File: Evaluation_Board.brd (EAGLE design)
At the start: 60.9 x 39.4 mm, 41 parts, among them IC1 MEGA32-A, IC2 FT232RL, IC3 317EMP, J1 DCJ0202

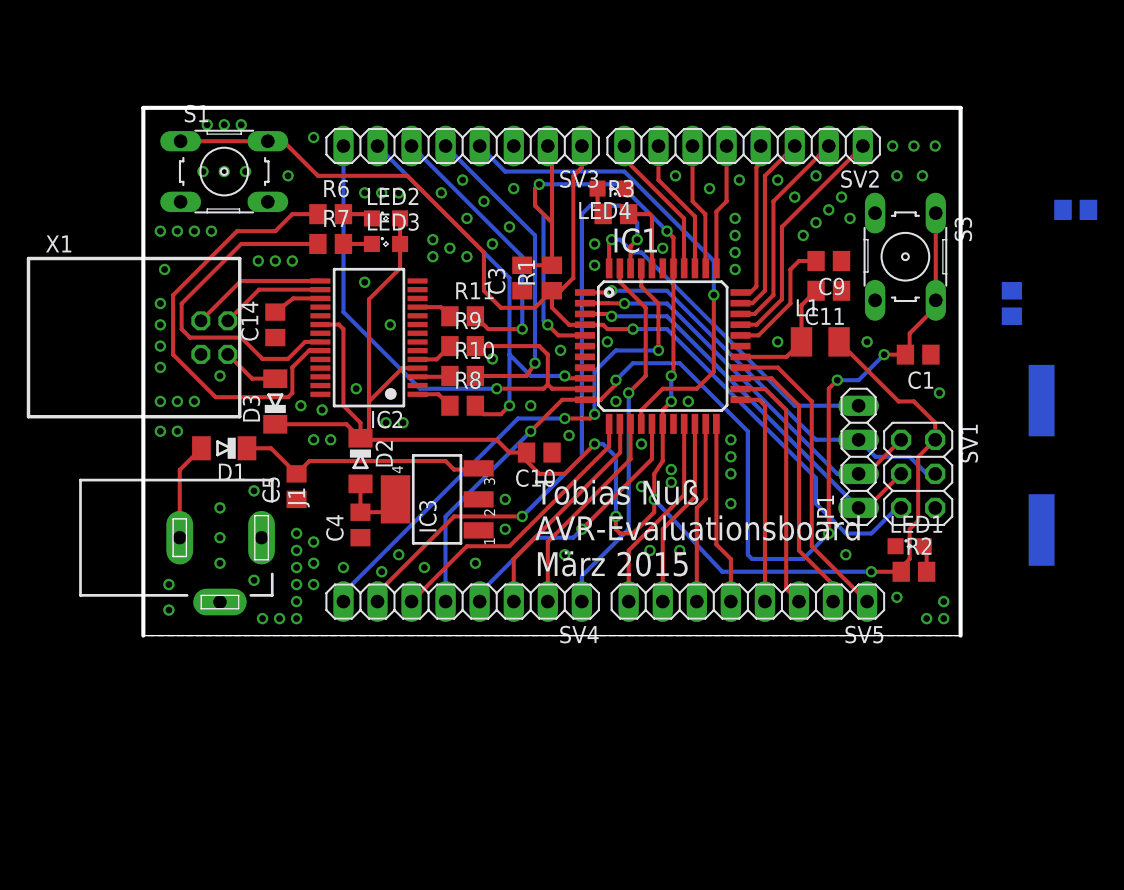
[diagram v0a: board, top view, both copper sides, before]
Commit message: Changed dimension layer to 0 mil -> standard for board outline. Smashed all components to move them and get a better silk screen.
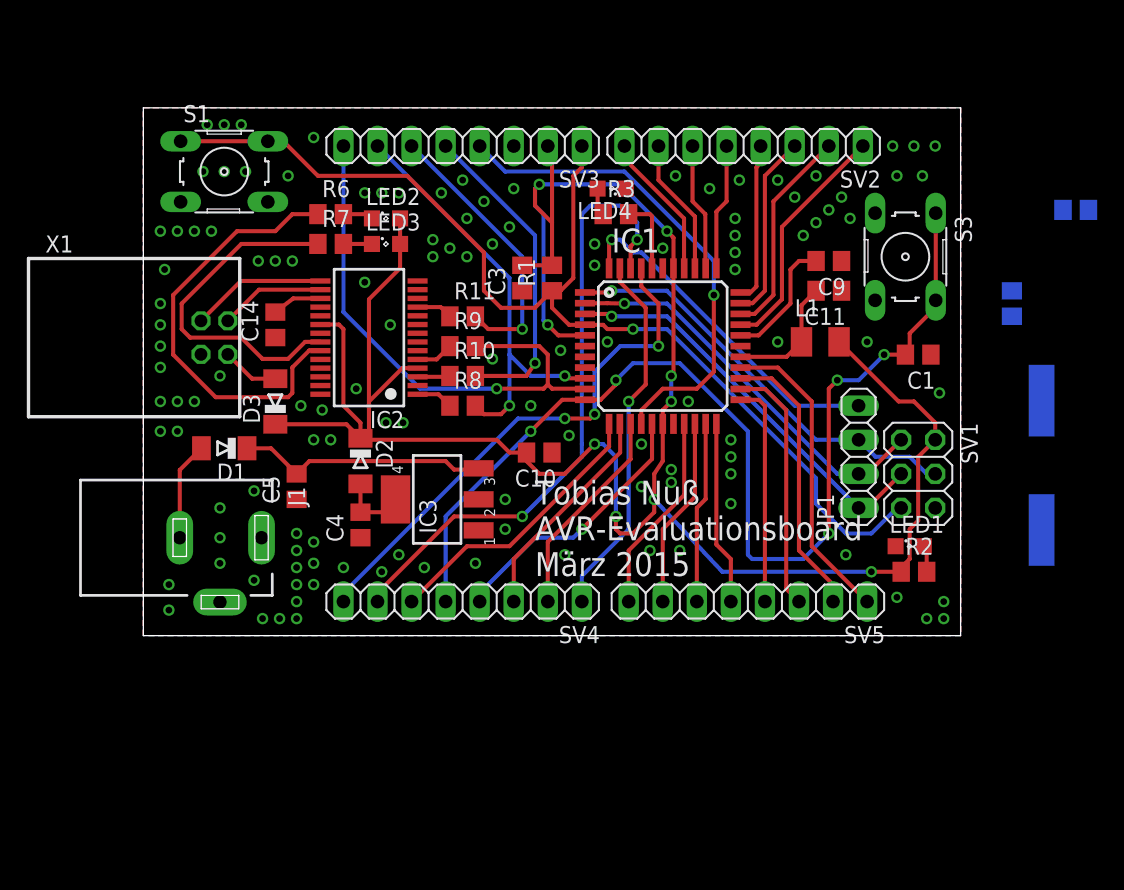
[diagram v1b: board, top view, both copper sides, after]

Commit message: Added crystal to layout and changed the values for both load caps.
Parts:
- C2, C6: value 100n -> 12p
- Q1: value (none) -> 16 MHz
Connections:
- new net N$17: C2.2, IC1.7, Q1.2
- new net N$25: C6.2, IC1.8, Q1.1
- net GND: now also C2.1, C6.1
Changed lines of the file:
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@@
 <attribute name="VALUE" x="12.2555" y="15.8115" size="1.27" layer="27" rot="R90"/>
 </element>
-<element name="C2" library="rcl" package="C0805" value="100n" x="64.77" y="24.765" smashed="yes" rot="MR270">
+<element name="C2" library="rcl" package="C0805" value="12p" x="64.77" y="24.765" smashed="yes" rot="MR270">
 <attribute name="NAME" x="63.5" y="26.035" size="1.27" layer="26" rot="MR270"/>
 <attribute name="VALUE" x="67.31" y="26.035" size="1.27" layer="28" rot="MR270"/>
 </element>
-<element name="C6" library="rcl" package="C0805" value="100n" x="69.5325" y="31.75" smashed="yes" rot="MR180">
+<element name="C6" library="rcl" package="C0805" value="12p" x="69.5325" y="31.75" smashed="yes" rot="MR180">
 <attribute name="NAME" x="68.2625" y="30.48" size="1.27" layer="26" rot="MR180"/>
 <attribute name="VALUE" x="68.2625" y="34.29" size="1.27" layer="28" rot="MR180"/>
 </element>
-<element name="Q1" library="crystal" package="HC49UP" value="" x="66.9925" y="12.7" smashed="yes" rot="MR90">
+<element name="Q1" library="crystal" package="HC49UP" value="16 MHz" x="66.9925" y="12.7" smashed="yes" rot="MR90">
 <attribute name="OC_NEWARK" value="unknown" x="66.9925" y="12.7" size="1.778" layer="28" rot="MR90" display="off"/>
 <attribute name="MPN" value="" x="66.9925" y="12.7" size="1.778" layer="28" rot="MR90" display="off"/>
@@
 <via x="37.1475" y="11.1125" extent="1-16" drill="0.5"/>
 <via x="38.735" y="28.8925" extent="1-16" drill="0.5"/>
+<contactref element="C2" pad="1"/>
+<contactref element="C6" pad="1"/>
+<wire x1="64.77" y1="25.715" x2="68.5825" y2="31.75" width="0" layer="19" extent="16-16"/>
+<wire x1="58.735" y1="20.955" x2="64.77" y2="25.715" width="0" layer="19" extent="1-16"/>
 </signal>
 <signal name="+5V">
@@
 <wire x1="17.8535" y1="9.205" x2="18.8085" y2="10.16" width="0.3048" layer="1"/>
 </signal>
+<signal name="N$17">
+<contactref element="Q1" pad="2"/>
+<contactref element="C2" pad="2"/>
+<contactref element="IC1" pad="7"/>
+<wire x1="66.9925" y1="17.526" x2="64.77" y2="23.815" width="0" layer="19" extent="16-16"/>
+<wire x1="32.935" y1="20.79" x2="64.77" y2="23.815" width="0" layer="19" extent="1-16"/>
+</signal>
+<signal name="N$25">
+<contactref element="Q1" pad="1"/>
+<contactref element="C6" pad="2"/>
+<contactref element="IC1" pad="8"/>
+<wire x1="66.9925" y1="7.874" x2="70.4825" y2="31.75" width="0" layer="19" extent="16-16"/>
+<wire x1="32.935" y1="19.99" x2="66.9925" y2="7.874" width="0" layer="19" extent="1-16"/>
+</signal>
 </signals>

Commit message: Begin of revolution! ;-)
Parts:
- removed R10, R11, R8, R9: 1k, rcl:R0805
- added C7: 100n, rcl:C0805
- moved Q1 43.4 mm to (25.4, 25.2), flipped to the top
- moved C6 40.3 mm to (30.8, 20.8), flipped to the top, turned to 270 degrees
- moved C2 35.4 mm to (29.4, 24.3), flipped to the top
- moved C3 17.2 mm to (33.2, 43.2)
- moved R1 17.2 mm to (35.4, 43.2)
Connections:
- removed net N$21: IC2.1, R8.1
- removed net N$22: IC2.5, R9.1
- removed net N$23: IC2.3, R10.1
- removed net N$24: IC2.11, R11.1
- net +5V: now also C7.2
- net CTS: now also IC2.11; no longer R11.2
- net GND: now also C7.1
- net RTS: now also IC2.3; no longer R10.2
- net RX_USB: now also IC2.1; no longer R8.2
- net TX_USB: now also IC2.5; no longer R9.2
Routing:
- net +5V: track 174.9 -> 129.4 mm, vias 9 -> 7
- net RESET: track 83.3 -> 38.4 mm
- net TX_USB: track 40.9 -> 0.00 mm, vias 1 -> 0
- net RX_USB: track 32.9 -> 0.00 mm, vias 2 -> 0
- net RTS: track 23.9 -> 0.00 mm, vias 1 -> 0
- net CTS: track 21.0 -> 0.00 mm, vias 1 -> 0
- net N$22: track 2.82 -> 0.00 mm
- net N$21: track 2.76 -> 0.00 mm
- net N$24: track 2.69 -> 0.00 mm
- net N$23: track 2.44 -> 0.00 mm
- net PD2_INT0: track 81.1 -> 82.0 mm

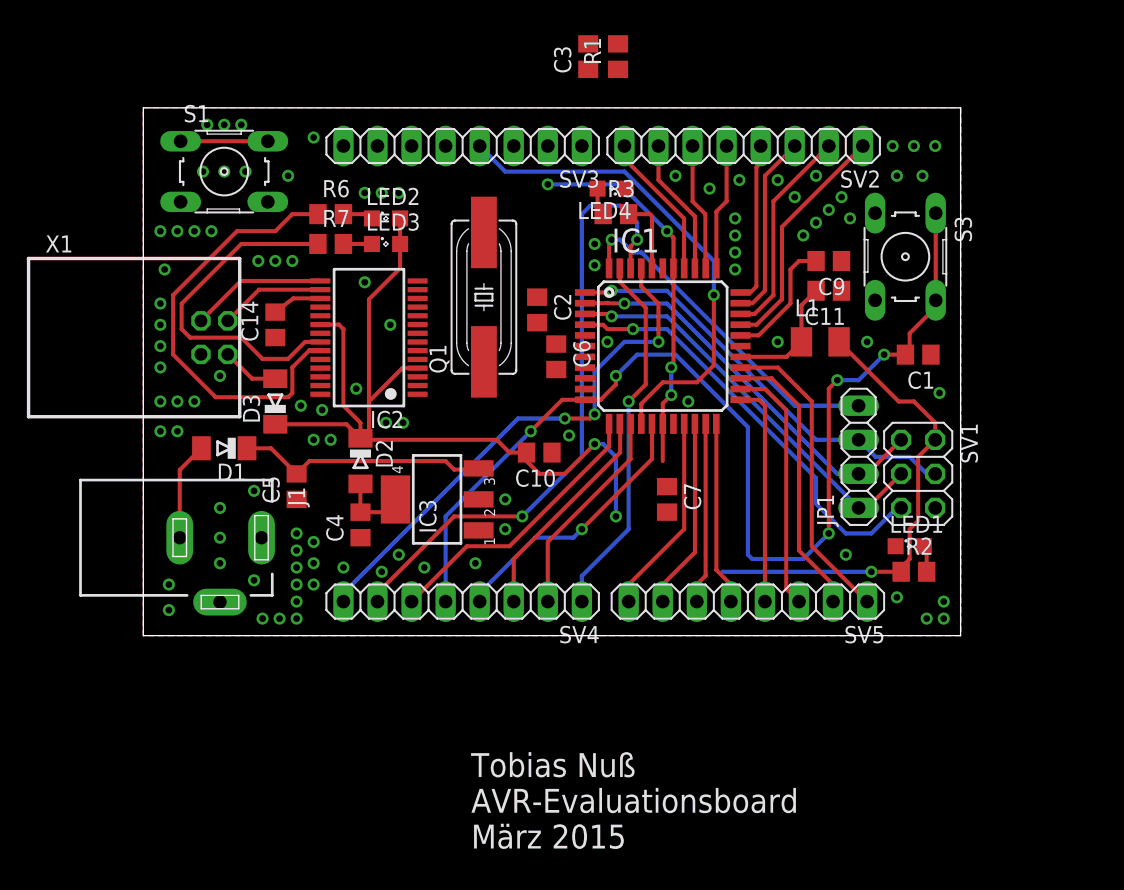
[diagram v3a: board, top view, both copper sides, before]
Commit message: No airwires left, implemented crystal layout and removed the resistors on serial line. Removed diode D2 from voltage regulator and placed as anti parallel diode.
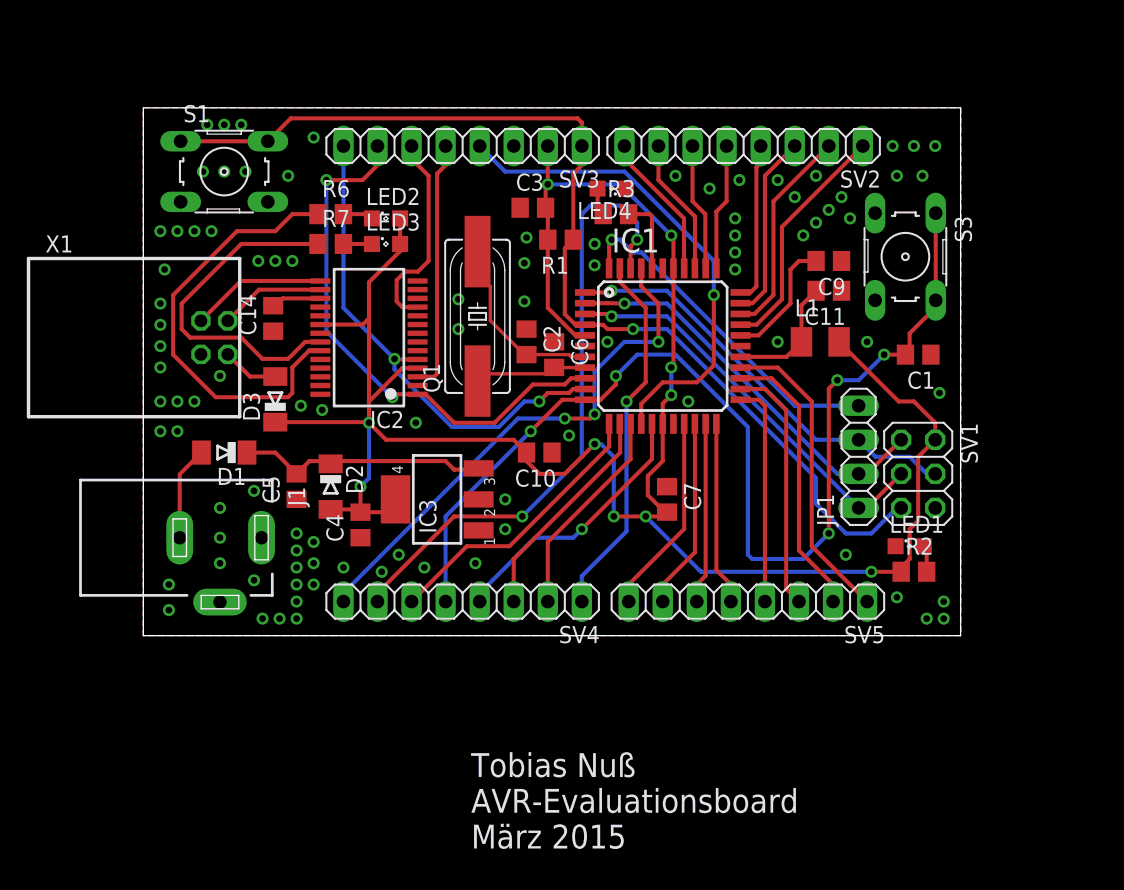
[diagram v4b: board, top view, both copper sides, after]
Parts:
- moved R1 14.3 mm to (31.1, 29.5), turned to 180 degrees
- moved C3 12.0 mm to (29.1, 31.9), turned to 0 degrees
- moved D2 2.93 mm to (14.0, 11.1)
- moved C2 2.51 mm to (28.6, 21.9)
- moved Q1 1.51 mm to (24.9, 23.8)
- moved C14 0.50 mm to (9.68, 23.7)
- moved D1 0.32 mm to (6.03, 13.7)
- moved C6 0.22 mm to (30.6, 21.0)
- moved D3 0.16 mm to (9.84, 17.6)
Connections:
- removed net N$2: C4.2, D2.A, IC3.4
- net +5V: now also C4.2, D2.A, IC3.4; no longer D2.C
- net NETZ: now also D2.C
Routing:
- net RESET: track 38.4 -> 79.3 mm
- net RX_USB: track 0.00 -> 40.6 mm, vias 0 -> 2
- net TX_USB: track 0.00 -> 37.4 mm, vias 0 -> 2
- net +5V: track 129.4 -> 165.6 mm, vias 7 -> 10
- net RTS: track 0.00 -> 18.8 mm
- net CTS: track 0.00 -> 15.4 mm
- net N$17: track 0.00 -> 13.9 mm
- net N$25: track 0.00 -> 8.82 mm
- net N$2: track 5.12 -> 0.00 mm

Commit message: Added measures. Placed all silk screen prints. PCB text now on bottom layer.
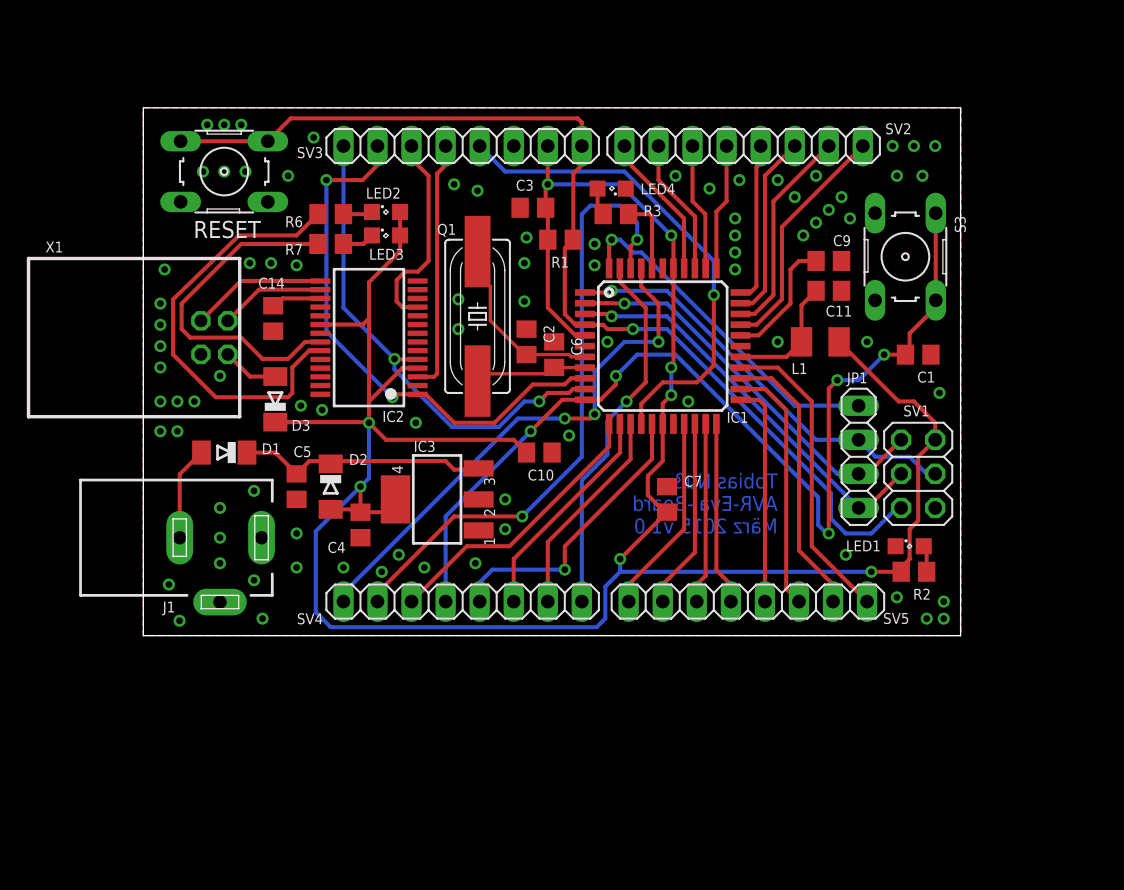
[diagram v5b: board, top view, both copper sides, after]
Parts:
- moved LED3 0.63 mm to (18.1, 29.8)
- moved LED2 0.48 mm to (18.1, 31.6)
- renumbered S1 to RESET
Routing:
- net +5V: track 165.6 -> 191.8 mm, vias 10 -> 8
- net PD2_INT0: track 82.0 -> 76.1 mm
- net OC2: track 20.2 -> 21.7 mm
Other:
- board text added: "Tobias Nuß AVR-Eval-Board März 2015 v1.0"
- board text removed: "Tobias Nuß AVR-Evaluationsboard März 2015"
